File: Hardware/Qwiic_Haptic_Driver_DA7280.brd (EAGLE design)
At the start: 25.4 x 29.2 mm, 49 parts, among them J1 QWIIC_RIGHT_ANGLE, J2 QWIIC_RIGHT_ANGLE, M1 G1040003D_LRA_CASTELLATED, U1 HAPTIC_DRIVER_DA7280

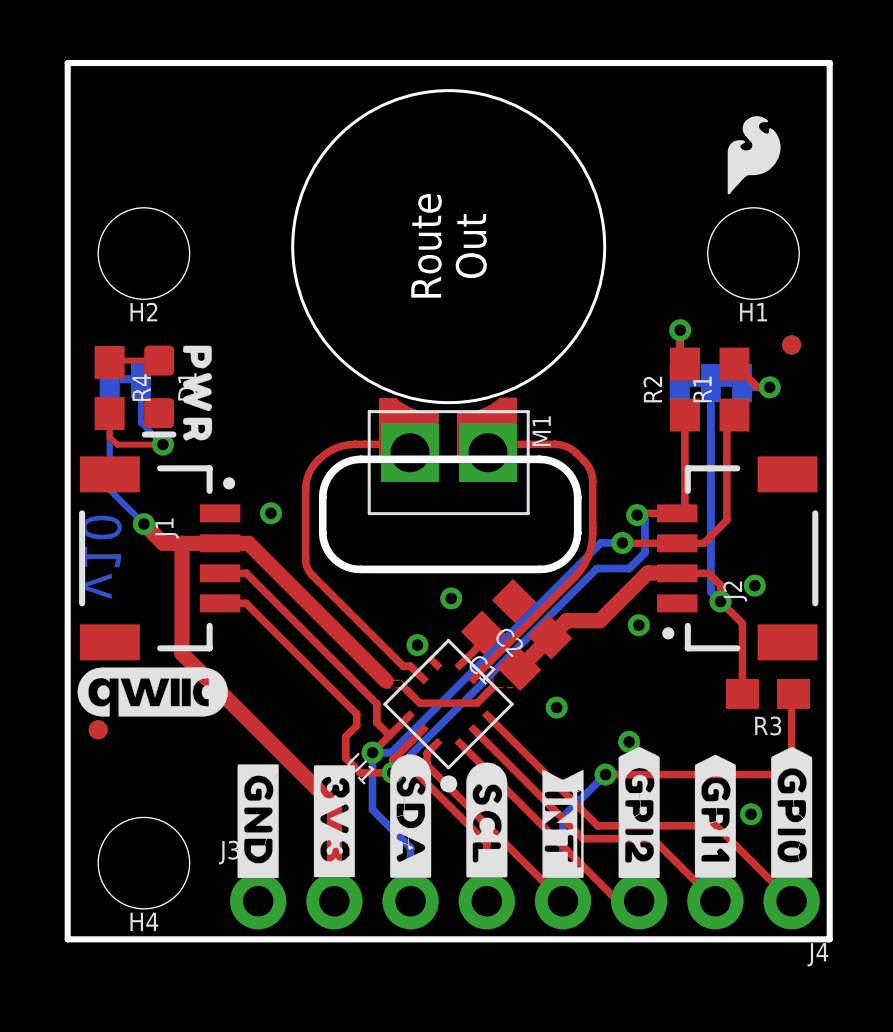
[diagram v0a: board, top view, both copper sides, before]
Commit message: Adds a jumper and plated through hole for separate VDDIO supply, adds silk for VDD
* Changes power symbols to VDD and VDDIO in place of 3V3
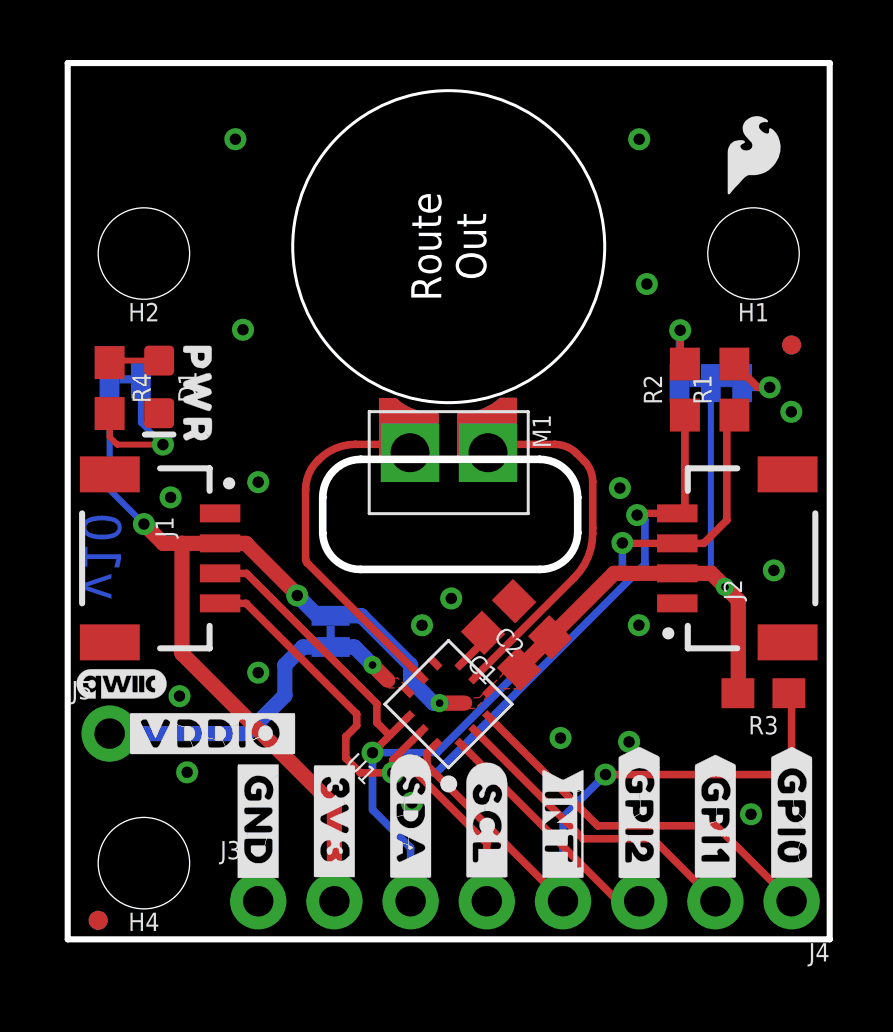
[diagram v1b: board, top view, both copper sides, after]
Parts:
- added J5: (no value), SparkFun-Connectors:1X01_NO_SILK
- added JP2: LED, SparkFun-Jumpers:SMT-JUMPER_2_NC_TRACE_SILK
- added LOGO1: SPECIAL_INSTRUCTIONS-ORDERING, SparkFun-Aesthetics:ORDERING_INSTRUCTIONS
- added U$15: (no value), top:#VDDIO#5
- added U$29: (no value), top:DA72809
- added U$30: (no value), top:#IO#6
- added U$7: (no value), top:#VDD#4
- U$1: value QWIIC_LOGO_5MM -> QWIIC_LOGO_3MM; device SparkFun-Aesthetics:QWIIC_5MM -> SparkFun-Aesthetics:QWIIC_3MM
- U$10: device top:HAPTIC7 -> top:MOTOR7
- U$11: device top:MOTOR_DRIVER8 -> top:DRIVER8
- U$25: device top:#3V3#1 -> top:#VDDIO#5
- U$9: device top:DA72809 -> top:HAPTIC6
- moved U$10 8.01 mm to (20.2, 9.53)
- moved U$9 6.46 mm to (17.4, 11.2)
- moved FD1 6.35 mm to (1.02, 0.64)
- moved FD2 6.35 mm to (1.02, 0.64)
- moved U$25 5.00 mm to (4.83, 6.86), turned to 0 degrees
- moved U$11 2.08 mm to (14.1, 9.40)
- moved U$1 1.05 mm to (1.79, 8.51)
- moved R3 0.15 mm to (23.2, 8.20)
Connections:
- removed net 3.3V: C1.1, C2.1, J1.2, J2.2, J3.2, JP1.2, JP3.2, R3.2, U1.P4, U1.P9
- new net VDD: C1.1, C2.1, J1.2, J2.2, J3.2, JP1.2, JP2.2, JP3.2, R3.2, U1.P4
- new net VDDIO: J5.1, JP2.1, U1.P9
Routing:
- net 3.3V: track 52.3 -> 0.00 mm, vias 2 -> 0
- net VDD: track 0.00 -> 51.9 mm, vias 0 -> 4
- net VDDIO: track 0.00 -> 11.5 mm, vias 0 -> 1
- net GND: vias 8 -> 19
- added copper zone on layer 1, net VDD
- added copper zone on layer 1, net VDDIO
- removed copper zone on layer 1, net 3.3V
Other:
- board text added: "Castellated Leads"

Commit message: Fixes some hidden airwires, approves some minor DRC errors
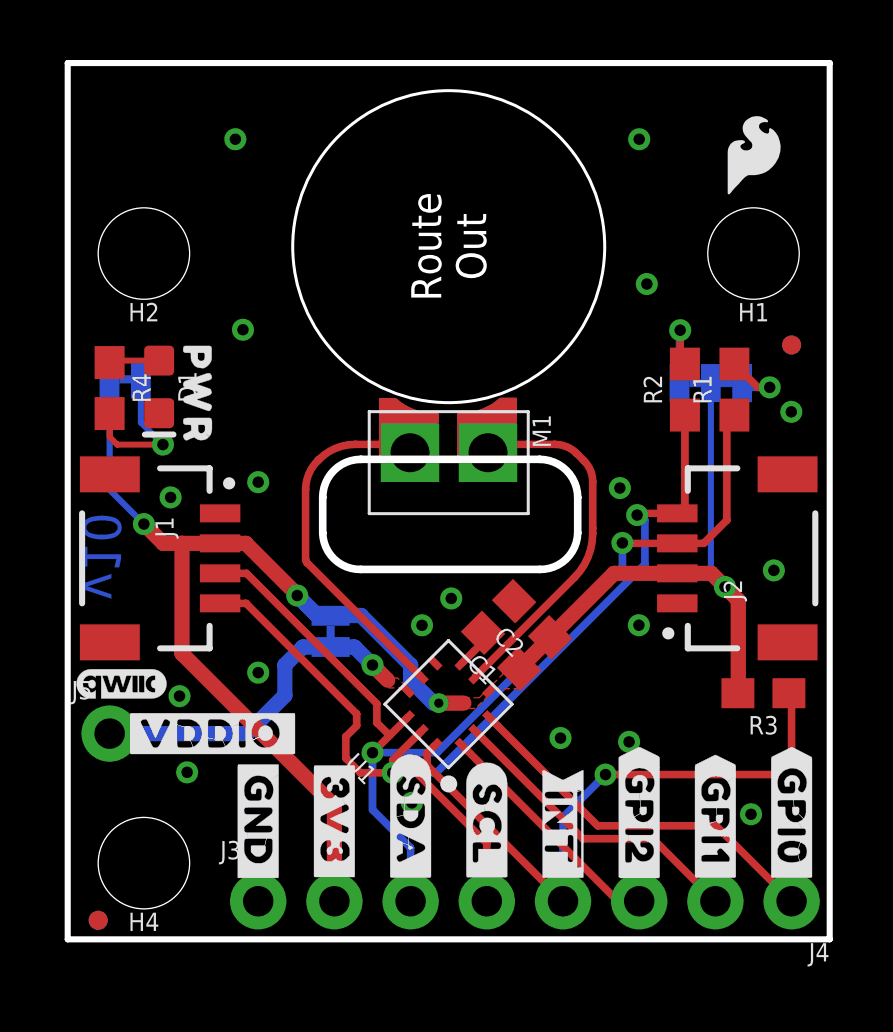
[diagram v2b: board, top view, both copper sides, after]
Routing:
- net VDD: track 51.9 -> 53.3 mm
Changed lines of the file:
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@@
 <contactref element="U1" pad="P4"/>
 <contactref element="JP2" pad="2"/>
-<via x="12.3952" y="7.874" extent="1-16" drill="0.254"/>
+<via x="12.3698" y="7.874" extent="1-16" drill="0.3048"/>
 <contactref element="JP1" pad="2"/>
 <contactref element="JP3" pad="2"/>
@@
 <wire x1="5.08" y1="13.2" x2="5.9370125" y2="13.2" width="0.508" layer="1"/>
 <wire x1="7.65080625" y1="11.46080625" x2="7.65080625" y2="11.48620625" width="0.508" layer="1"/>
-<wire x1="7.65080625" y1="11.46080625" x2="7.73798125" y2="11.46080625" width="0.508" layer="16"/>
 <contactref element="J2" pad="2"/>
 <contactref element="J3" pad="2"/>
@@
 <wire x1="18.211284375" y1="12.2" x2="20.32" y2="12.2" width="0.508" layer="1"/>
 <wire x1="15.0464375" y1="9.017346875" x2="16.081840625" y2="10.05275" width="0.508" layer="1"/>
-<wire x1="12.3952" y1="7.874" x2="13.2334" y2="7.874" width="0.508" layer="1"/>
+<wire x1="12.3698" y1="7.874" x2="13.208" y2="7.874" width="0.508" layer="1"/>
 <wire x1="5.08" y1="13.2" x2="3.81" y2="13.2" width="0.508" layer="1"/>
 <polygon width="0.127" layer="1" isolate="0.3048" thermals="no">
@@
 <wire x1="11.43" y1="8.636" x2="11.43" y2="9.144" width="0.508" layer="16"/>
 <wire x1="11.43" y1="8.636" x2="12.192" y2="7.874" width="0.508" layer="16"/>
-<wire x1="12.192" y1="7.874" x2="12.3952" y2="7.874" width="0.508" layer="16"/>
+<wire x1="12.192" y1="7.874" x2="12.3698" y2="7.874" width="0.508" layer="16"/>
 <wire x1="21.4376" y1="18.542" x2="21.4376" y2="12.2174" width="0.2032" layer="16"/>
 <wire x1="21.4376" y1="12.2174" x2="21.9075" y2="11.7475" width="0.2032" layer="16"/>
-<via x="21.9075" y="11.7475" extent="1-16" drill="0.254"/>
+<via x="21.9075" y="11.7475" extent="1-16" drill="0.381"/>
 <wire x1="1.397" y1="14.986" x2="1.397" y2="18.669" width="0.2032" layer="16"/>
-<wire x1="8.5397125" y1="10.795" x2="8.47175" y2="10.7270375" width="0.508" layer="16"/>
-<wire x1="7.65080625" y1="11.46080625" x2="8.3166125" y2="10.795" width="0.508" layer="16"/>
-<wire x1="8.3166125" y1="10.795" x2="8.5397125" y2="10.795" width="0.508" layer="16"/>
-<wire x1="11.43" y1="9.144" x2="9.7880875" y2="10.7859125" width="0.508" layer="16"/>
-<wire x1="9.7880875" y1="10.7859125" x2="8.763" y2="10.7859125" width="0.508" layer="16"/>
-<wire x1="8.763" y1="10.7859125" x2="8.47175" y2="10.7270375" width="0" layer="19" extent="16-16"/>
+<wire x1="8.3166125" y1="10.795" x2="7.65080625" y2="11.46080625" width="0.508" layer="16"/>
+<wire x1="11.43" y1="9.144" x2="9.779" y2="10.795" width="0.508" layer="16"/>
+<wire x1="9.779" y1="10.795" x2="8.3166125" y2="10.795" width="0.508" layer="16"/>
+<wire x1="8.763" y1="10.7859125" x2="8.3257" y2="10.7859125" width="0.508" layer="16"/>
+<wire x1="8.3257" y1="10.7859125" x2="7.65080625" y2="11.46080625" width="0.508" layer="16"/>
 </signal>
 <signal name="VDDIO">
 <contactref element="U1" pad="P9"/>
 <contactref element="JP2" pad="1"/>
-<via x="10.16" y="9.144" extent="1-16" drill="0.254"/>
+<via x="10.16" y="9.144" extent="1-16" drill="0.381"/>
 <wire x1="10.16" y1="9.144" x2="10.668" y2="8.636" width="0.508" layer="1"/>
 <polygon width="0.127" layer="1" isolate="0.3048" thermals="no">

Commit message: Adds Jumpers for separating VDDIO from VDD and Qwiic bus voltage from the board
* Updates measures
* Adds OSHW and SparkFun logo to board
* Adds text to jumpers in the schematic
* Updates symbol to use short legs
* Adds VDD and VDDIO range
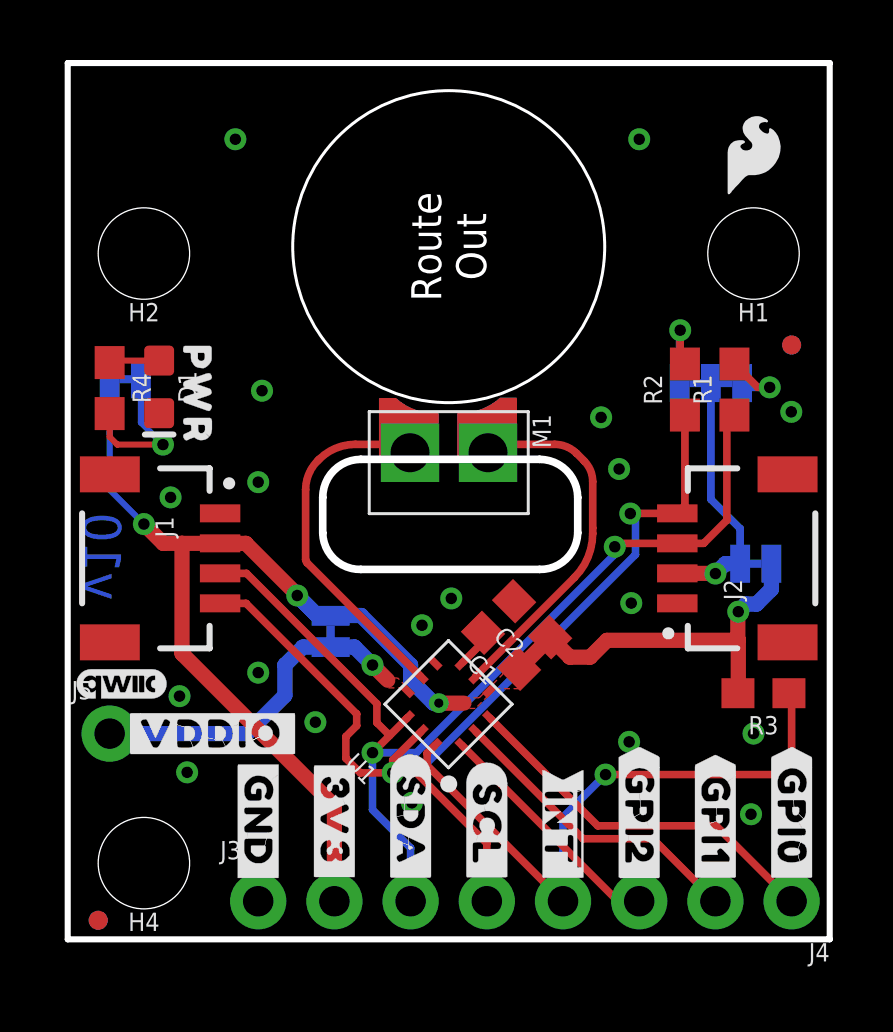
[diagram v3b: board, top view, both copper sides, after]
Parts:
- removed U$22: (no value), SparkFun-Aesthetics:OSHW-LOGO-MINI
- added JP4: LED, SparkFun-Jumpers:SMT-JUMPER_2_NC_TRACE_SILK
- added LOGO2: OSHW-LOGOS, SparkFun-Aesthetics:OSHW-LOGO-S
- added U$31: (no value), bot:#QISO#0
- LOGO4: value (none) -> SFE_LOGO_FLAME.1_INCH
- renumbered U$17 to LOGO4
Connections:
- new net QWIIC_BUS: J2.2, JP3.2, JP4.1
- net VDD: now also JP4.2; no longer J2.2, JP3.2
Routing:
- net QWIIC_BUS: track 0.00 -> 8.66 mm, vias 0 -> 1
- net VDD: track 53.3 -> 47.5 mm

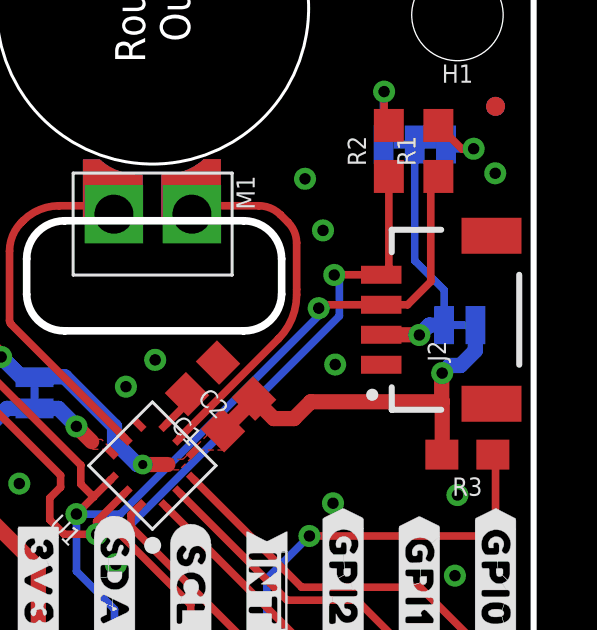
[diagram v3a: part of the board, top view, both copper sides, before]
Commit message: Approves some minor DRC errors
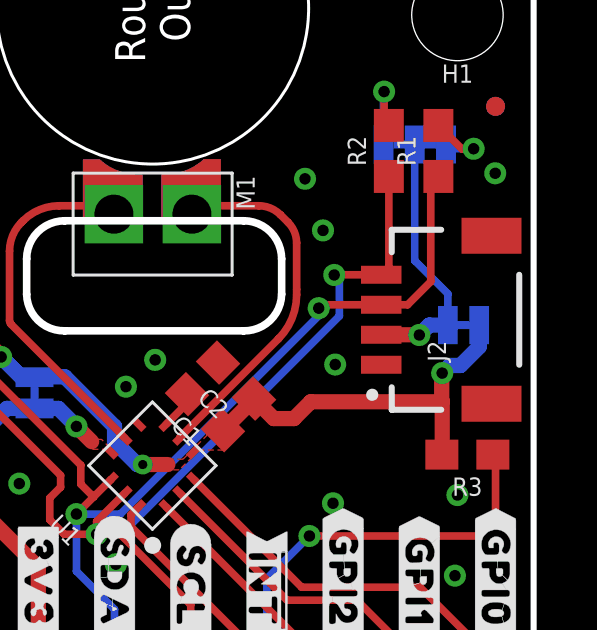
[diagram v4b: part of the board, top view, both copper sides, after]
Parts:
- moved JP4 0.13 mm to (23.1, 12.5)
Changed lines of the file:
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@@
 <setting verticaltext="up"/>
 </settings>
-<grid distance="0.01" unitdist="inch" unit="inch" style="dots" multiple="1" display="yes" altdistance="0.001" altunitdist="inch" altunit="inch"/>
+<grid distance="0.05" unitdist="inch" unit="inch" style="dots" multiple="1" display="yes" altdistance="0.005" altunitdist="inch" altunit="inch"/>
 <layers>
 <layer number="1" name="Top" color="4" fill="1" visible="yes" active="yes"/>
@@
 <layer number="115" name="ReferenceISLANDS" color="7" fill="1" visible="no" active="no"/>
 <layer number="116" name="Patch_BOT" color="9" fill="4" visible="no" active="no"/>
-<layer number="117" name="PM_Ref" color="26" fill="1" visible="no" active="yes"/>
+<layer number="117" name="PM_Ref" color="26" fill="1" visible="yes" active="yes"/>
 <layer number="118" name="Rect_Pads" color="7" fill="1" visible="no" active="no"/>
-<layer number="119" name="PF_Ref" color="31" fill="1" visible="no" active="yes"/>
-<layer number="120" name="WFL_Ref" color="25" fill="1" visible="no" active="yes"/>
+<layer number="119" name="PF_Ref" color="31" fill="1" visible="yes" active="yes"/>
+<layer number="120" name="WFL_Ref" color="25" fill="1" visible="yes" active="yes"/>
 <layer number="121" name="_tsilk" color="7" fill="1" visible="no" active="no"/>
 <layer number="122" name="_bsilk" color="7" fill="1" visible="no" active="no"/>
@@
 <element name="U$29" library="top" package="DA72809" value="" x="17.399" y="7.747" smashed="yes" rot="MR0"/>
 <element name="U$30" library="top" package="#IO#6" value="" x="6.604" y="10.287" smashed="yes" rot="MR0"/>
-<element name="JP4" library="SparkFun-Jumpers" package="SMT-JUMPER_2_NC_TRACE_SILK" package3d_urn="urn:adsk.eagle:package:39281/1" value="LED" x="22.9362" y="12.5222" smashed="yes" rot="MR180">
-<attribute name="NAME" x="22.9362" y="11.3792" size="0.6096" layer="26" font="vector" ratio="20" rot="MR180" align="bottom-center"/>
-<attribute name="VALUE" x="22.9362" y="13.6652" size="0.6096" layer="28" font="vector" ratio="20" rot="MR180" align="top-center"/>
+<element name="JP4" library="SparkFun-Jumpers" package="SMT-JUMPER_2_NC_TRACE_SILK" package3d_urn="urn:adsk.eagle:package:39281/1" value="LED" x="23.0632" y="12.5222" smashed="yes" rot="MR180">
+<attribute name="NAME" x="23.0632" y="11.3792" size="0.6096" layer="26" font="vector" ratio="20" rot="MR180" align="bottom-center"/>
+<attribute name="VALUE" x="23.0632" y="13.6652" size="0.6096" layer="28" font="vector" ratio="20" rot="MR180" align="top-center"/>
 </element>
 <element name="U$31" library="bot" package="#QISO#0" value="" x="22.606" y="14.2494" smashed="yes" rot="MR0"/>
@@
 <wire x1="22.352" y1="10.922" x2="22.606" y2="11.176" width="0.508" layer="16"/>
 <wire x1="22.606" y1="11.176" x2="22.9616" y2="11.176" width="0.508" layer="16"/>
-<wire x1="22.9616" y1="11.176" x2="23.4569" y2="11.6713" width="0.508" layer="16"/>
-<wire x1="23.4569" y1="11.6713" x2="23.4569" y2="12.5222" width="0.508" layer="16"/>
+<wire x1="22.9616" y1="11.176" x2="23.5839" y2="11.7983" width="0.508" layer="16"/>
+<wire x1="23.5839" y1="11.7983" x2="23.5839" y2="12.5222" width="0.508" layer="16"/>
 </signal>
 <signal name="VDDIO">
@@
 <via x="21.59" y="12.192" extent="1-16" drill="0.381"/>
 <wire x1="21.59" y1="12.192" x2="21.9202" y2="12.5222" width="0.508" layer="16"/>
-<wire x1="21.9202" y1="12.5222" x2="22.4155" y2="12.5222" width="0.508" layer="16"/>
+<wire x1="21.9202" y1="12.5222" x2="22.5425" y2="12.5222" width="0.508" layer="16"/>
 <contactref element="JP3" pad="2"/>
-<wire x1="22.4155" y1="12.5222" x2="22.4155" y2="13.6906" width="0.254" layer="16"/>
-<wire x1="22.4155" y1="13.6906" x2="21.4376" y2="14.6685" width="0.254" layer="16"/>
+<wire x1="22.5425" y1="12.5222" x2="22.5425" y2="13.5636" width="0.254" layer="16"/>
+<wire x1="22.5425" y1="13.5636" x2="21.4376" y2="14.6685" width="0.254" layer="16"/>
 <wire x1="21.4376" y1="14.6685" x2="21.4376" y2="18.542" width="0.254" layer="16"/>
 </signal>

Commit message: Adds second qwiic connecter to "qwiic bus" net so that the respective jumper can disconnect both
* Adds some power symbols
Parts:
- moved JP2 0.34 mm to (8.69, 9.94)
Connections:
- net QWIIC_BUS: now also J1.2
- net VDD: no longer J1.2
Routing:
- net QWIIC_BUS: track 8.84 -> 30.1 mm, vias 1 -> 2
- net VDD: track 47.6 -> 44.7 mm
